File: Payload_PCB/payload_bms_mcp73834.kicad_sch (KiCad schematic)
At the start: 11 parts, among them U3 MCP73834-FCI/UN

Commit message: Minor changes and corrections
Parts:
- added BT1: Samsung INR18650-35E, symbol Device:Battery_Cell
- renumbered C7 to C16, C8 to C17, D11 to D20, D10 to D21, D9 to D22, R16 to R49, R15 to R50, R14 to R51, R18 to R52, U3 to U9
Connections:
- net GND: now also BT1.2 (-)
- net VBAT+: now also BT1.1 (+)
- net VDD renamed VIN_BMS

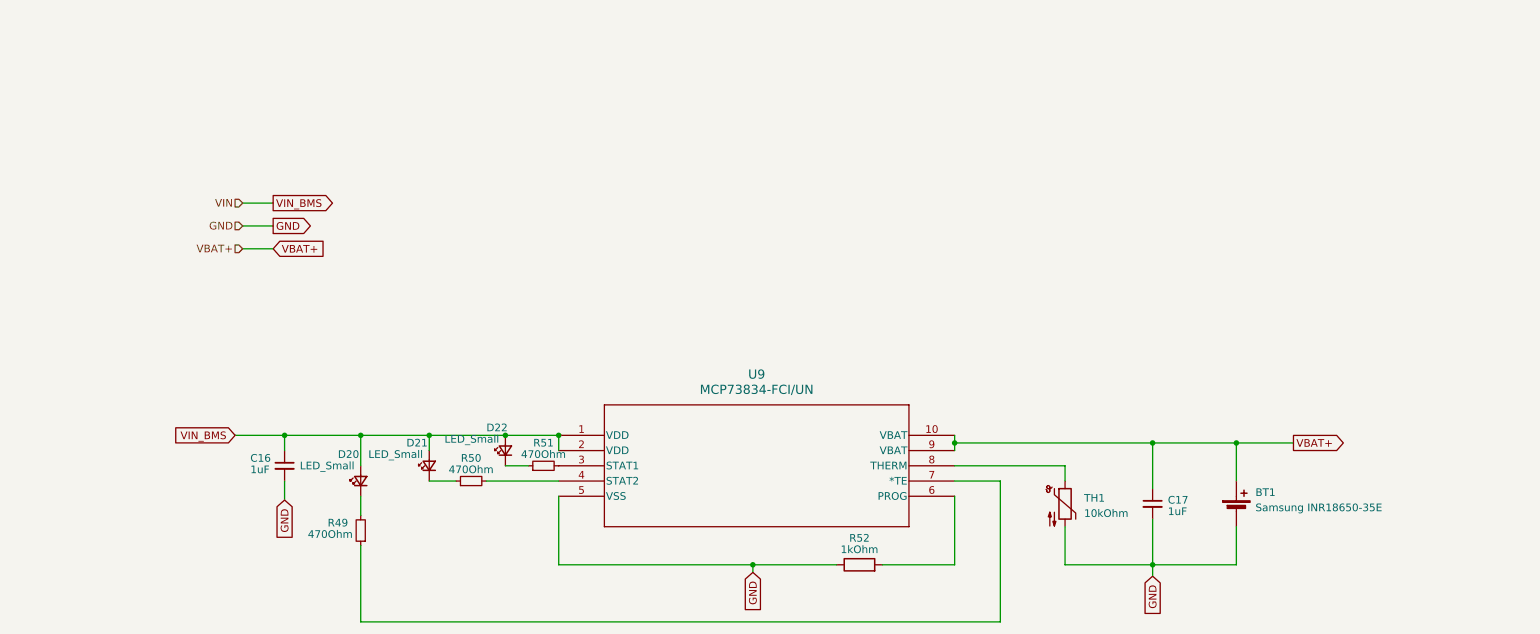
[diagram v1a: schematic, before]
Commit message: Add BMS Chip and Radio Silence
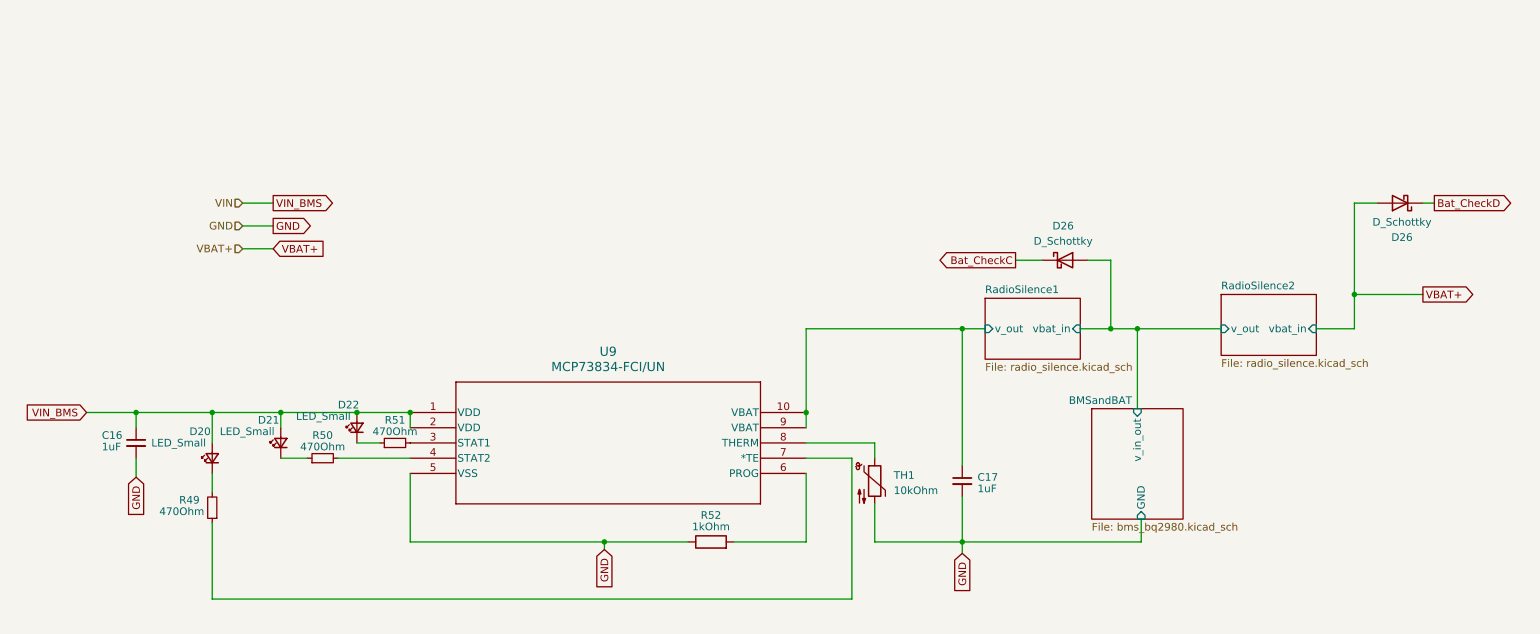
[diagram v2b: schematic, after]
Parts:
- removed BT1: Samsung INR18650-35E, symbol Device:Battery_Cell
- added D26 (x2): D_Schottky, symbol Device:D_Schottky
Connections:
- net VBAT+: now also D26.2 (A); no longer C17.1, U9.10 (VBAT), U9.9 (VBAT)
- new net BMSandBAT/v_in_out: D26.2 (A)
- new net Bat_CheckC: D26.1 (K)
- new net Bat_CheckD: D26.1 (K)
- new net RadioSilence1/v_out: C17.1, U9.10 (VBAT), U9.9 (VBAT)
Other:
- added sheet BMSandBAT (bms_bq2980.kicad_sch)
- added sheet RadioSilence1 (radio_silence.kicad_sch)
- added sheet RadioSilence2 (radio_silence.kicad_sch)
- moved on the sheet: C16, C17, D20, D21, D22, R49, R50, R51, R52, TH1, U9

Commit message: Added some actual parts
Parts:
- removed D20, D21, D22: LED_Small, symbol Device:LED_Small
- removed D26 (x2): D_Schottky, symbol Device:D_Schottky
- added LED1, LED3: TLUR2400, TLUR2400, symbol TLUR2400:TLUR2400
- added LED5: TLUG2400, TLUG2400, symbol TLUG2400:TLUG2400
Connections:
- net VIN_BMS: now also LED1.2 (A), LED3.2 (A), LED5.2 (A)
- net at R49.2: now also LED5.1 (K)
- net at R50.1: now also LED3.1 (K)
- net at R51.1: now also LED1.1 (K)
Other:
- note added: "Green"
- note added: "Red"
- company: (none) -> SpaceTeam Aachen
- title: (none) -> Battery Charge & Discharge

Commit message: Change to actual real parts
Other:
- sheet RadioSilence1 ports: added v_in; removed vbat_in
- sheet RadioSilence2 ports: added v_in; removed vbat_in
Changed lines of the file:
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@@
       (effects (font (size 1.27 1.27)) (justify left))
     )
-    (pin "vbat_in" input (at 240.665 73.66 0)
+    (pin "v_in" input (at 240.665 73.66 0)
       (effects (font (size 1.27 1.27)) (justify right))
     )
@@
       (effects (font (size 1.27 1.27)) (justify left))
     )
-    (pin "vbat_in" input (at 201.295 73.66 0)
+    (pin "v_in" input (at 201.295 73.66 0)
       (effects (font (size 1.27 1.27)) (justify right))
     )

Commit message: some new parts
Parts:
- LED1, LED3: footprint TLUR2400 -> footprints:TLUR2400
- LED5: footprint TLUG2400 -> footprints:TLUG2400
- U9: footprint MSOP10_MC_MCH -> MCP73834-FCI_UN:MSOP10_MC_MCH
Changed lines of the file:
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@@
   (junction (at 181.61 73.66) (diameter 0) (color 0 0 0 0)
   )
-  (junction (at 247.015 67.945) (diameter 0) (color 0 0 0 0)
+  (junction (at 237.49 67.945) (diameter 0) (color 0 0 0 0)
   )
   (junction (at 206.375 73.66) (diameter 0) (color 0 0 0 0)
@@
     (stroke (width 0) (type default))
   )
-  (wire (pts (xy 210.82 73.66) (xy 224.79 73.66))
+  (wire (pts (xy 210.82 73.66) (xy 215.265 73.66))
     (stroke (width 0) (type default))
   )
@@
     (stroke (width 0) (type default))
   )
-  (wire (pts (xy 247.015 67.945) (xy 258.445 67.945))
+  (wire (pts (xy 237.49 67.945) (xy 248.92 67.945))
     (stroke (width 0) (type default))
   )
@@
     (stroke (width 0) (type default))
   )
-  (wire (pts (xy 247.015 52.705) (xy 247.015 67.945))
+  (wire (pts (xy 237.49 52.705) (xy 237.49 67.945))
     (stroke (width 0) (type default))
   )
@@
     (stroke (width 0) (type default))
   )
-  (wire (pts (xy 240.665 73.66) (xy 247.015 73.66))
+  (wire (pts (xy 231.14 73.66) (xy 237.49 73.66))
     (stroke (width 0) (type default))
   )
@@
     (stroke (width 0) (type default))
   )
-  (wire (pts (xy 247.015 52.705) (xy 255.905 52.705))
+  (wire (pts (xy 237.49 52.705) (xy 246.38 52.705))
     (stroke (width 0) (type default))
   )
@@
     (stroke (width 0) (type default))
   )
-  (wire (pts (xy 247.015 73.66) (xy 247.015 67.945))
+  (wire (pts (xy 237.49 73.66) (xy 237.49 67.945))
     (stroke (width 0) (type default))
   )
@@
     )
   )
-  (global_label "VBAT+" (shape output) (at 258.445 67.945 0) (fields_autoplaced)
+  (global_label "VBAT+" (shape output) (at 248.92 67.945 0) (fields_autoplaced)
     (effects (font (size 1.27 1.27)) (justify left))
-    (property "Intersheetrefs" "${INTERSHEET_REFS}" (at 267.4174 67.945 0)
+    (property "Intersheetrefs" "${INTERSHEET_REFS}" (at 257.8924 67.945 0)
       (effects (font (size 1.27 1.27)) (justify left) hide)
     )
@@
     )
   )
-  (global_label "Bat_CheckD" (shape output) (at 255.905 52.705 0) (fields_autoplaced)
+  (global_label "Bat_CheckD" (shape output) (at 246.38 52.705 0) (fields_autoplaced)
     (effects (font (size 1.27 1.27)) (justify left))
-    (property "Intersheetrefs" "${INTERSHEET_REFS}" (at 269.8968 52.705 0)
+    (property "Intersheetrefs" "${INTERSHEET_REFS}" (at 260.3718 52.705 0)
       (effects (font (size 1.27 1.27)) (justify left) hide)
     )
@@
       (effects (font (size 1.27 1.27)) (justify right))
     )
-    (property "Footprint" "TLUG2400" (at 150.165 87.9475 0)
+    (property "Footprint" "footprints:TLUG2400" (at 150.165 87.9475 0)
       (effects (font (size 1.27 1.27)) (justify left bottom) hide)
     )
@@
       (effects (font (size 1.27 1.27)) (justify right))
     )
-    (property "Footprint" "TLUR2400" (at 174.295 83.82 0)
+    (property "Footprint" "footprints:TLUR2400" (at 174.295 83.82 0)
       (effects (font (size 1.27 1.27)) (justify left bottom) hide)
     )
@@
       (effects (font (size 1.27 1.27)) (justify right))
     )
-    (property "Footprint" "TLUR2400" (at 161.595 86.36 0)
+    (property "Footprint" "footprints:TLUR2400" (at 161.595 86.36 0)
       (effects (font (size 1.27 1.27)) (justify left bottom) hide)
     )
@@
       (effects (font (size 1.524 1.524)))
     )
-    (property "Footprint" "MSOP10_MC_MCH" (at 101.6 80.645 0)
+    (property "Footprint" "MCP73834-FCI_UN:MSOP10_MC_MCH" (at 101.6 80.645 0)
       (effects (font (size 1.27 1.27) italic) hide)
     )
@@
     )
   )
-  (sheet (at 224.79 67.945) (size 15.875 10.16) (fields_autoplaced)
+  (sheet (at 215.265 67.945) (size 15.875 10.16) (fields_autoplaced)
     (stroke (width 0.1524) (type solid))
     (fill (color 0 0 0 0.0000))
-    (property "Sheetname" "RadioSilence2" (at 224.79 67.2334 0)
+    (property "Sheetname" "RadioSilence2" (at 215.265 67.2334 0)
       (effects (font (size 1.27 1.27)) (justify left bottom))
     )
-    (property "Sheetfile" "radio_silence.kicad_sch" (at 224.79 78.6896 0)
+    (property "Sheetfile" "radio_silence.kicad_sch" (at 215.265 78.6896 0)
       (effects (font (size 1.27 1.27)) (justify left top))
     )
-    (property "Field2" "" (at 224.79 67.945 0)
-      (effects (font (size 1.27 1.27)) hide)
-    )
-    (pin "v_out" input (at 224.79 73.66 180)
-      (effects (font (size 1.27 1.27)) (justify left))
-    )
-    (pin "v_in" input (at 240.665 73.66 0)
-      (effects (font (size 1.27 1.27)) (justify right))
-    )
-    (instances
-      (project "Payload_PCB"
-        (path "/5c4f9a68-5778-4223-b18a-2e31db8d7d40/a5d6e803-a43d-4b6f-b631-9dac7ff20cfd" (page "17"))
-        (path "/5c4f9a68-5778-4223-b18a-2e31db8d7d40/722fc623-9945-41d5-bc31-e6d0e92574b1" (page "19"))
+    (property "Field2" "" (at 215.265 67.945 0)
+      (effects (font (size 1.27 1.27)) hide)
+    )
+    (pin "v_out" input (at 215.265 73.66 180)
+      (effects (font (size 1.27 1.27)) (justify left))
+    )
+    (pin "v_in" input (at 231.14 73.66 0)
+      (effects (font (size 1.27 1.27)) (justify right))
+    )
+    (instances
+      (project "Payload_PCB"
+        (path "/5c4f9a68-5778-4223-b18a-2e31db8d7d40/a5d6e803-a43d-4b6f-b631-9dac7ff20cfd" (page "15"))
+        (path "/5c4f9a68-5778-4223-b18a-2e31db8d7d40/722fc623-9945-41d5-bc31-e6d0e92574b1" (page "18"))
       )
     )
@@
     (instances
       (project "Payload_PCB"
-        (path "/5c4f9a68-5778-4223-b18a-2e31db8d7d40/a5d6e803-a43d-4b6f-b631-9dac7ff20cfd" (page "18"))
+        (path "/5c4f9a68-5778-4223-b18a-2e31db8d7d40/a5d6e803-a43d-4b6f-b631-9dac7ff20cfd" (page "16"))
+        (path "/5c4f9a68-5778-4223-b18a-2e31db8d7d40/722fc623-9945-41d5-bc31-e6d0e92574b1" (page "20"))
       )
     )
@@
     (instances
       (project "Payload_PCB"
-        (path "/5c4f9a68-5778-4223-b18a-2e31db8d7d40/a5d6e803-a43d-4b6f-b631-9dac7ff20cfd" (page "16"))
-      )
-    )
+        (path "/5c4f9a68-5778-4223-b18a-2e31db8d7d40/a5d6e803-a43d-4b6f-b631-9dac7ff20cfd" (page "14"))
+        (path "/5c4f9a68-5778-4223-b18a-2e31db8d7d40/722fc623-9945-41d5-bc31-e6d0e92574b1" (page "19"))
+      )
+    )

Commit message: Todo notes after review
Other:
- note added: "RadioSilence1 kann theoretisch rausgeschmissen werden"
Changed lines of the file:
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@@
     (effects (font (size 0.508 0.508)) (justify left bottom))
+  )
+  (text "RadioSilence1 kann theoretisch rausgeschmissen werden"
+    (at 145.415 57.15 0)
+    (effects (font (size 1.27 1.27)) (justify left bottom))
   )
   (text "Red" (at 78.74 93.345 0)

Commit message: first parts layout
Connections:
- net RadioSilence1/v_out is gone; now on net Bat_CheckC: C17.1, U9.10 (VBAT), U9.9 (VBAT)
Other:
- removed sheet RadioSilence1
- note added: "Output for Radio Silence"
- note added: "RadioSilence1 raus, weil eh keine Ladung bei Radio Silence"
- note removed: "RadioSilence1 kann theoretisch rausgeschmissen werden"
- moved on the sheet: C16, C17, LED1, LED3, LED5, R49, R50, R51, R52, TH1, U9
